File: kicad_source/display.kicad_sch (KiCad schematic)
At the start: 3 parts, among them J1 Conn_01x08

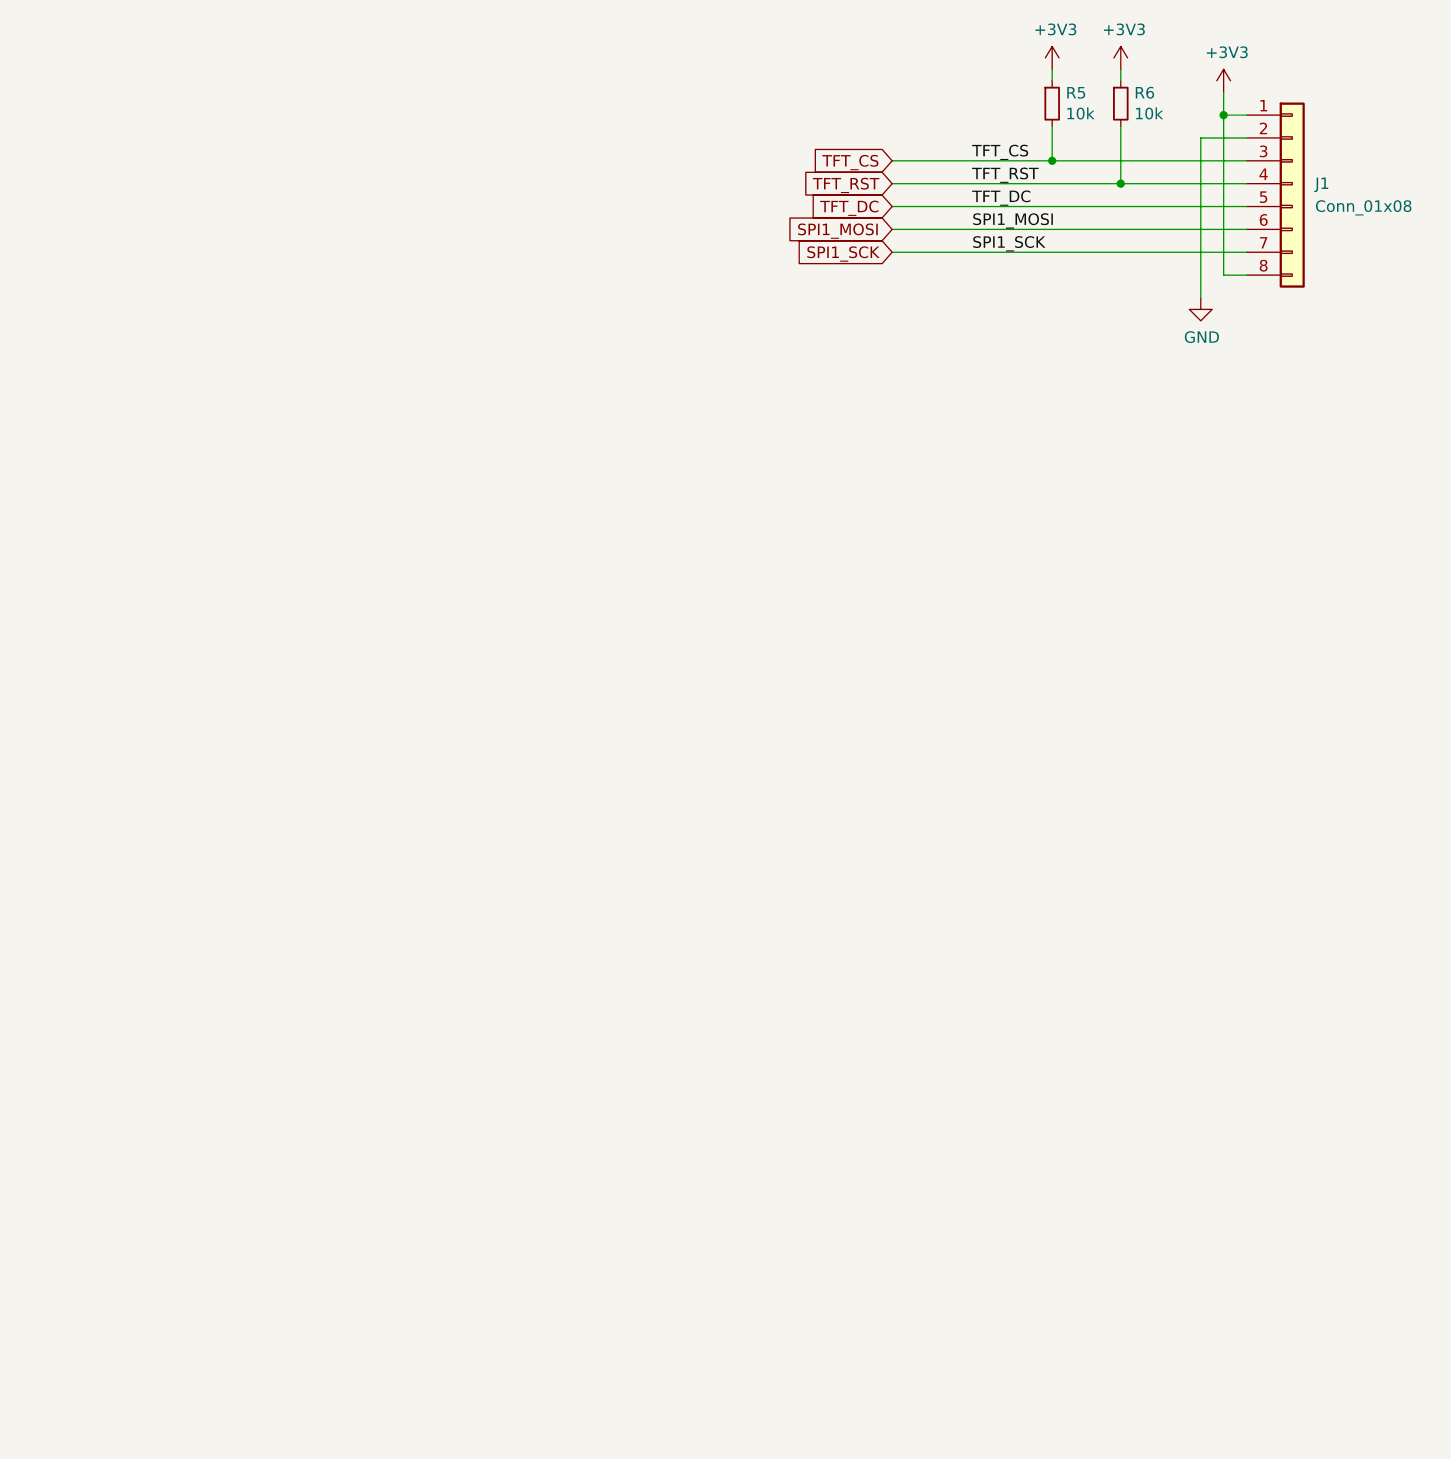
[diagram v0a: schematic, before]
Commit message: added encoder, mounting holes for display at correct position
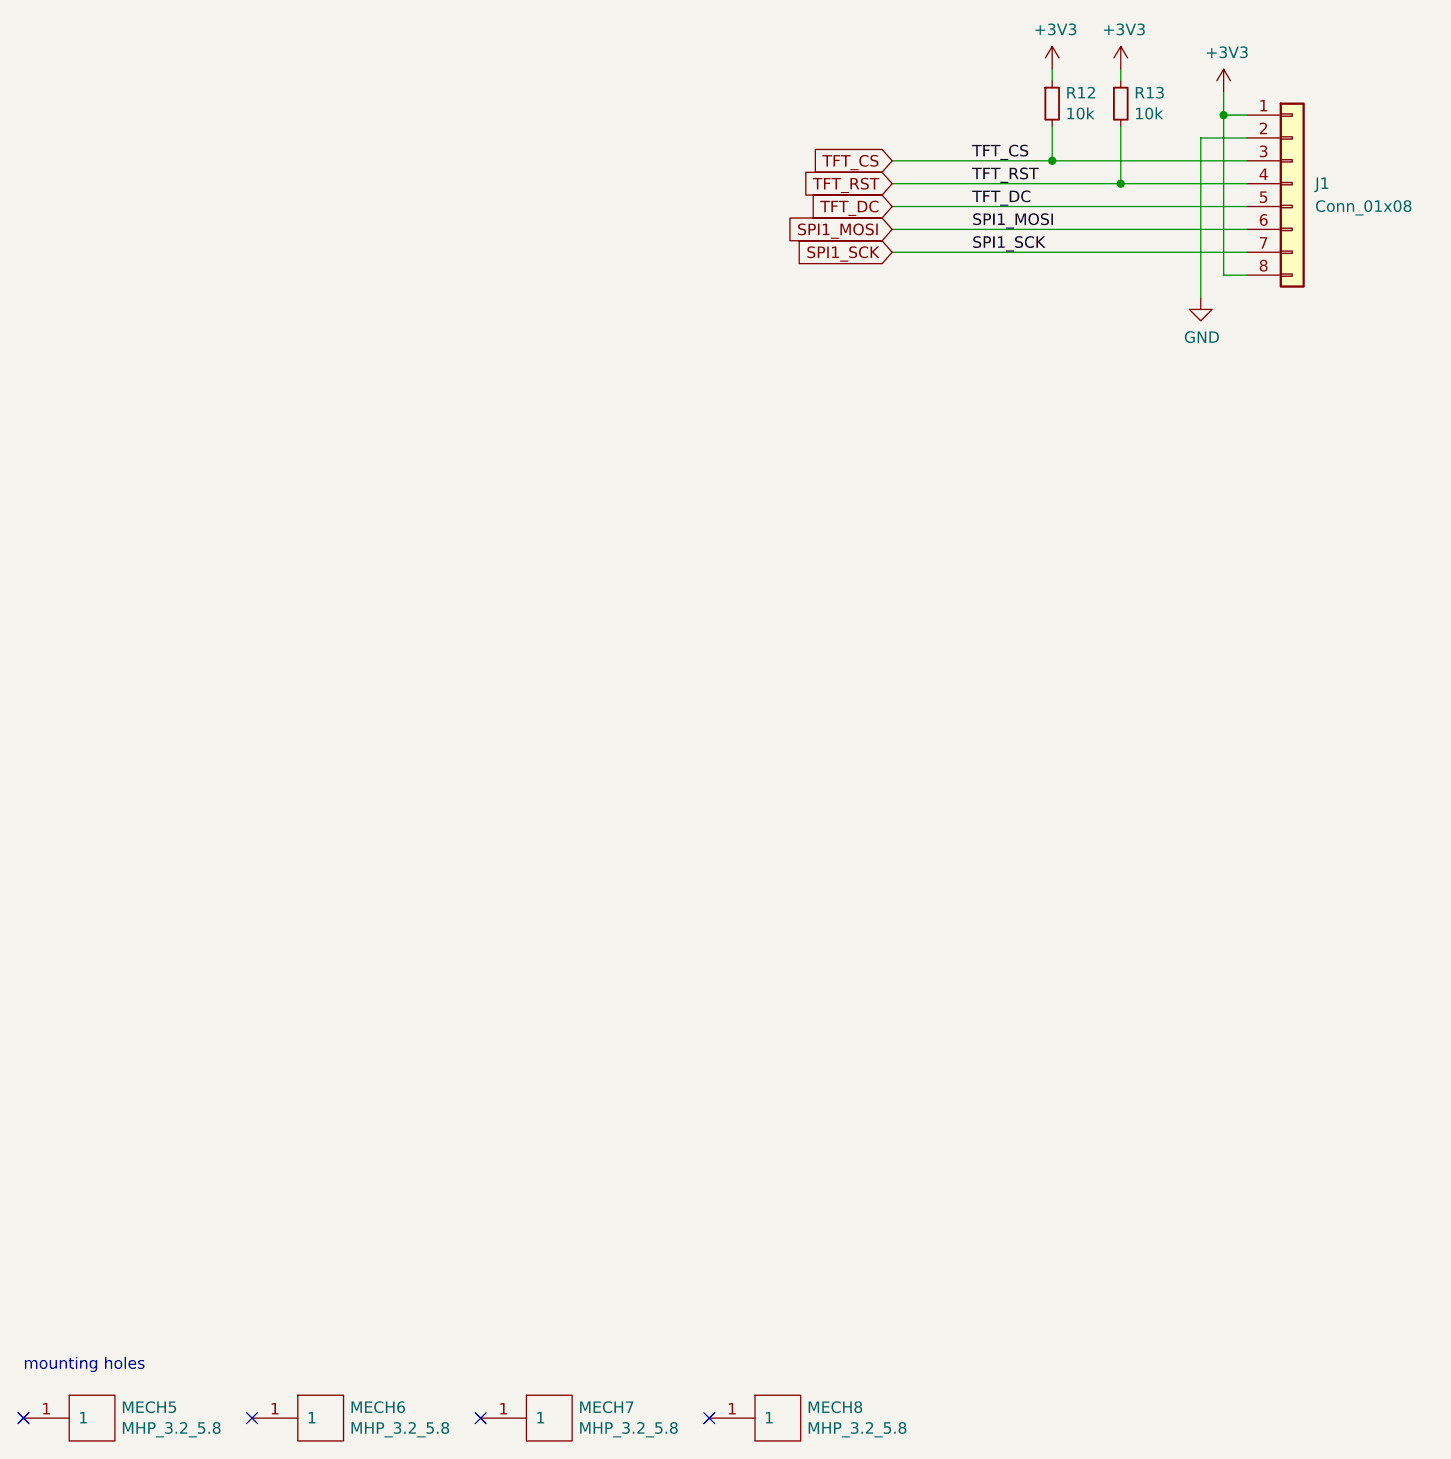
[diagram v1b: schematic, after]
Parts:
- removed R5, R6: 10k, Resistor_SMD:R_0603_1608Metric, symbol Device:R_Small
- added MECH5, MECH6, MECH7, MECH8: MHP_3.2_5.8, MountingHole:MountingHole_3.2mm_M3_ISO14580_Pad, symbol OpenCyphalPicoBase-rescue:MHP_3.2_5.8-MECH_mounting-holes
- added R12, R13: 10k, Resistor_SMD:R_0603_1608Metric, symbol Device:R_Small
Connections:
- net +3V3: now also R12.1, R13.1
- net TFT_CS: now also R12.2
- net TFT_RST: now also R13.2
- no-connect marks 0 -> 4
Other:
- note added: "mounting holes"
